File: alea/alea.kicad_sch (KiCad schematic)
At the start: 47 parts, among them J1 QL_SLOT_DIN41612, J2 Conn_02x17_Odd_Even, J3 Conn_01x03_Pin, Q1 BC109, U0 LM340T-5, U1 68000D, U10 MSM514400D, U11 MSM514400D, U12 DP4873V, U2 EP1810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

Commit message: 2025/06 update
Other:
- moved on the sheet: BT1, C1, C2, D1, D2, D3, H1, H2, Q1, R1, R2, U7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

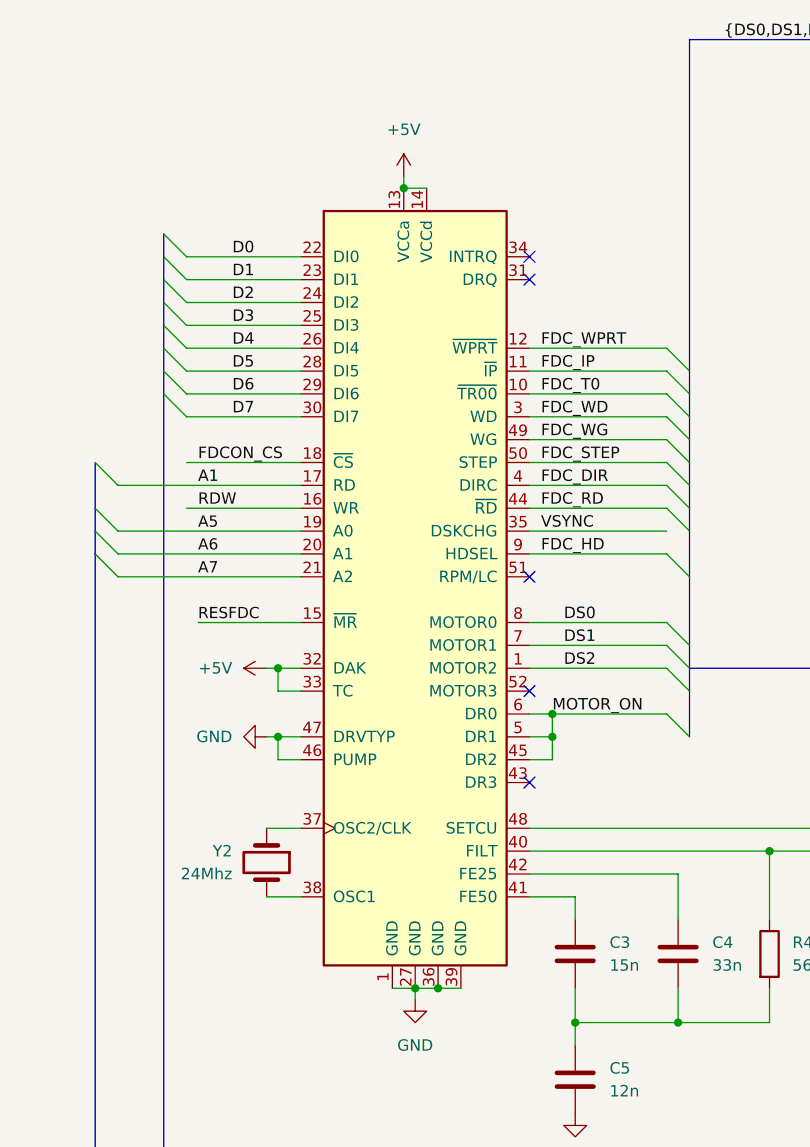
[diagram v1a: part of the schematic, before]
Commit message: update again for bad FDC pinout
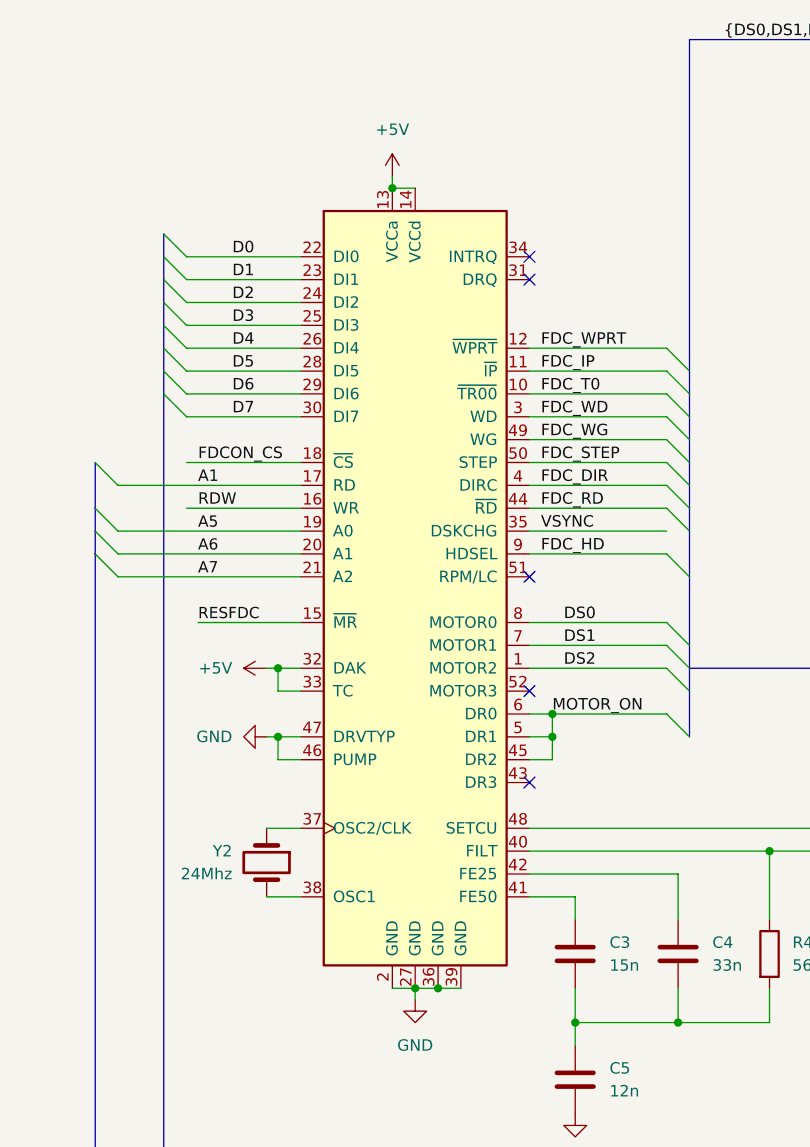
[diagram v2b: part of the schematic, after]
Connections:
- net GND: now also U12.2 (GND); no longer U12.1 (MOTOR2)
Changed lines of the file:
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@@
 	)
 	(junction
-		(at 209.55 81.28)
+		(at 85.09 66.04)
 		(diameter 0)
 		(color 0 0 0 0)
 	)
 	(junction
-		(at 266.7 161.29)
+		(at 209.55 81.28)
 		(diameter 0)
 		(color 0 0 0 0)
 	)
 	(junction
-		(at 86.36 66.04)
+		(at 266.7 161.29)
 		(diameter 0)
 		(color 0 0 0 0)
@@
 	(wire
 		(pts
-			(xy 86.36 64.77) (xy 86.36 66.04)
+			(xy 85.09 64.77) (xy 85.09 66.04)
 		)
 		(stroke
@@
 	(wire
 		(pts
-			(xy 86.36 66.04) (xy 88.9 66.04)
+			(xy 85.09 66.04) (xy 87.63 66.04)
 		)
 		(stroke
@@
 	(symbol
 		(lib_id "GoldCard_Library:+5V")
-		(at 86.36 64.77 0)
+		(at 85.09 64.77 0)
 		(unit 1)
 		(exclude_from_sim no)
@@
 		(fields_autoplaced yes)
 		(property "Reference" "#PWR038"
-			(at 86.36 68.58 0)
+			(at 85.09 68.58 0)
 			(effects
 				(font
@@
 		)
 		(property "Value" "+5V"
-			(at 86.36 59.5376 0)
+			(at 85.09 59.5376 0)
 			(effects
 				(font
@@
 		)
 		(property "Footprint" ""
-			(at 86.36 64.77 0)
+			(at 85.09 64.77 0)
 			(effects
 				(font
@@
 		)
 		(property "Datasheet" ""
-			(at 86.36 64.77 0)
+			(at 85.09 64.77 0)
 			(effects
 				(font
@@
 		)
 		(property "Description" ""
-			(at 86.36 64.77 0)
+			(at 85.09 64.77 0)
 			(effects
 				(font
@@
 		(pin "9"
 		)
-		(pin "1"
+		(pin "2"
 		)
 		(pin "27"

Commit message: fix values
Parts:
- added C17: 100n, Capacitor_THT:C_Disc_D4.3mm_W1.9mm_P5.00mm, symbol GoldCard_Library:C
- C1, C2: value C -> 22p
- Q1: value BC109 -> BC548
- R1, R2: value R -> 1K
- Y3: value Crystal -> 32768hz
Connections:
- net +5V: now also C17.1
- net GND: now also U6.18 (B0)
- net at D1.2 (A), D2.2 (A), U7.8 (GND): now also C17.2
- no-connect marks 43 -> 42
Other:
- title: Sinclair QL Gold Card 3 -> Sinclair QL Gold Card 4 (ALEA's Version)

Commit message: small update in alea
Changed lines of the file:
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@@
 	)
 	(junction
+		(at 64.77 215.9)
+		(diameter 0)
+		(color 0 0 0 0)
+	)
+	(junction
 		(at 209.55 81.28)
 		(diameter 0)
@@
 	)
 	(junction
-		(at 133.35 220.98)
-		(diameter 0)
-		(color 0 0 0 0)
-	)
-	(junction
 		(at 130.81 368.3)
 		(diameter 0)
@@
 	)
 	(junction
-		(at 125.73 220.98)
-		(diameter 0)
-		(color 0 0 0 0)
-	)
-	(junction
 		(at 209.55 114.3)
 		(diameter 0)
@@
 	)
 	(junction
+		(at 64.77 213.36)
+		(diameter 0)
+		(color 0 0 0 0)
+	)
+	(junction
 		(at 35.56 340.36)
 		(diameter 0)
@@
 	)
 	(bus_entry
-		(at 137.16 220.98)
-		(size -2.54 2.54)
-		(stroke
-			(width 0)
-			(type default)
-		)
-	)
-	(bus_entry
 		(at 452.12 81.28)
 		(size 2.54 2.54)
@@
 	)
 	(bus_entry
-		(at 137.16 215.9)
-		(size -2.54 2.54)
-		(stroke
-			(width 0)
-			(type default)
-		)
-	)
-	(bus_entry
 		(at 452.12 125.73)
 		(size 2.54 2.54)
@@
 	)
 	(bus_entry
-		(at 137.16 218.44)
-		(size -2.54 2.54)
-		(stroke
-			(width 0)
-			(type default)
-		)
-	)
-	(bus_entry
 		(at 52.07 238.76)
 		(size 2.54 2.54)
@@
 	(bus
 		(pts
-			(xy 137.16 220.98) (xy 137.16 222.25)
+			(xy 137.16 219.71) (xy 137.16 222.25)
 		)
 		(stroke
@@
 	(wire
 		(pts
-			(xy 54.61 215.9) (xy 92.71 215.9)
+			(xy 54.61 215.9) (xy 64.77 215.9)
 		)
 		(stroke
@@
 		)
 	)
-	(bus
-		(pts
-			(xy 137.16 218.44) (xy 137.16 219.71)
-		)
-		(stroke
-			(width 0)
-			(type default)
-		)
-	)
 	(wire
 		(pts
@@
 		)
 	)
-	(wire
-		(pts
-			(xy 133.35 220.98) (xy 133.35 227.33)
-		)
-		(stroke
-			(width 0)
-			(type default)
-		)
-	)
 	(bus
 		(pts
@@
 		)
 	)
-	(wire
-		(pts
-			(xy 125.73 220.98) (xy 125.73 218.44)
-		)
-		(stroke
-			(width 0)
-			(type default)
-		)
-	)
 	(bus
 		(pts
@@
 		)
 	)
+	(wire
+		(pts
+			(xy 64.77 213.36) (xy 64.77 215.9)
+		)
+		(stroke
+			(width 0)
+			(type default)
+		)
+	)
 	(bus
 		(pts
@@
 		)
 	)
-	(wire
-		(pts
-			(xy 133.35 220.98) (xy 134.62 220.98)
-		)
-		(stroke
-			(width 0)
-			(type default)
-		)
-	)
 	(bus
 		(pts
@@
 	(wire
 		(pts
+			(xy 64.77 215.9) (xy 64.77 222.25)
+		)
+		(stroke
+			(width 0)
+			(type default)
+		)
+	)
+	(wire
+		(pts
 			(xy 407.67 148.59) (xy 420.37 148.59)
 		)
@@
 		)
 	)
+	(wire
+		(pts
+			(xy 64.77 215.9) (xy 92.71 215.9)
+		)
+		(stroke
+			(width 0)
+			(type default)
+		)
+	)
 	(bus
 		(pts
@@
 	(wire
 		(pts
-			(xy 125.73 220.98) (xy 133.35 220.98)
-		)
-		(stroke
-			(width 0)
-			(type default)
-		)
-	)
-	(wire
-		(pts
 			(xy 454.66 270.51) (xy 467.36 270.51)
 		)
@@
 	(wire
 		(pts
-			(xy 54.61 213.36) (xy 92.71 213.36)
+			(xy 54.61 213.36) (xy 64.77 213.36)
 		)
 		(stroke
@@
 		)
 	)
-	(wire
-		(pts
-			(xy 125.73 218.44) (xy 134.62 218.44)
-		)
-		(stroke
-			(width 0)
-			(type default)
-		)
-	)
 	(bus
 		(pts
@@
 		)
 	)
-	(bus
-		(pts
-			(xy 137.16 219.71) (xy 137.16 220.98)
-		)
-		(stroke
-			(width 0)
-			(type default)
-		)
-	)
 	(wire
 		(pts
@@
 		)
 	)
-	(bus
-		(pts
-			(xy 137.16 215.9) (xy 137.16 217.17)
-		)
-		(stroke
-			(width 0)
-			(type default)
-		)
-	)
 	(wire
 		(pts
@@
 	(bus
 		(pts
-			(xy 137.16 214.63) (xy 137.16 215.9)
+			(xy 137.16 214.63) (xy 137.16 217.17)
 		)
 		(stroke
@@
 	(wire
 		(pts
+			(xy 64.77 213.36) (xy 92.71 213.36)
+		)
+		(stroke
+			(width 0)
+			(type default)
+		)
+	)
+	(wire
+		(pts
 			(xy 50.8 344.17) (xy 63.5 344.17)
 		)
@@
 	(bus
 		(pts
-			(xy 137.16 217.17) (xy 137.16 218.44)
+			(xy 137.16 217.17) (xy 137.16 219.71)
 		)
 		(stroke
@@
 		)
 	)
-	(label "A19"
-		(at 129.54 220.98 0)
-		(effects
-			(font
-				(size 1.27 1.27)
-			)
-			(justify left bottom)
-		)
-	)
 	(label "MA5"
 		(at 410.21 151.13 0)
@@
 		)
 	)
-	(label "A18"
-		(at 129.54 218.44 0)
-		(effects
-			(font
-				(size 1.27 1.27)
-			)
-			(justify left bottom)
-		)
-	)
 	(label "RDL"
 		(at 346.71 97.79 0)
@@
 	(symbol
 		(lib_id "GoldCard_Library:GND")
-		(at 133.35 227.33 0)
+		(at 125.73 220.98 90)
 		(unit 1)
 		(exclude_from_sim no)
@@
 		(dnp no)
 		(property "Reference" "#PWR07"
-			(at 133.35 233.68 0)
+			(at 132.08 220.98 0)
 			(effects
 				(font
@@
 		)
 		(property "Value" "GND"
-			(at 135.128 231.14 0)
+			(at 122.682 219.964 90)
 			(effects
 				(font
@@
 		)
 		(property "Footprint" ""
-			(at 133.35 227.33 0)
+			(at 125.73 220.98 0)
 			(effects
 				(font
@@
 		)
 		(property "Datasheet" ""
-			(at 133.35 227.33 0)
+			(at 125.73 220.98 0)
 			(effects
 				(font
@@
 		)
 		(property "Description" ""
-			(at 133.35 227.33 0)
+			(at 125.73 220.98 0)
 			(effects
 				(font
@@
 					(unit 1)
 				)
+			)
+		)
+	)
+	(symbol
+		(lib_id "GoldCard_Library:GND")
+		(at 64.77 222.25 0)
+		(unit 1)
+		(exclude_from_sim no)
+		(in_bom yes)
+		(on_board yes)
+		(dnp no)
+		(property "Reference" "#PWR057"
+			(at 64.77 228.6 0)
+			(effects
+				(font
+					(size 1.27 1.27)
+				)
+				(hide yes)
+			)
+		)
+		(property "Value" "GND"
+			(at 66.548 226.06 0)
+			(effects
+				(font
+					(size 1.27 1.27)
+				)
+				(justify right)
+			)
+		)
+		(property "Footprint" ""
+			(at 64.77 222.25 0)
+			(effects
+				(font
+					(size 1.27 1.27)
+				)
+				(hide yes)
+			)
+		)
+		(property "Datasheet" ""
+			(at 64.77 222.25 0)
+			(effects
+				(font
+					(size 1.27 1.27)
+				)
+				(hide yes)
+			)
+		)
+		(property "Description" ""
+			(at 64.77 222.25 0)
+			(effects
+				(font
+					(size 1.27 1.27)
+				)
+				(hide yes)
+			)
+		)
+		(pin "1"
+		)
+		(instances
+			(project "alea"
+				(path "/aecd9f77-969e-41c8-a7ad-8348a70f1d7d"
+					(reference "#PWR057")
+					(unit 1)
+				)

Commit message: small update in alea
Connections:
- net DG0: now also U8.25 (D3); no longer U8.1 (D0)
- net DG1: now also U8.24 (D2); no longer U8.25 (D3)
- net DG2: now also U8.1 (D0); no longer U8.2 (D1)
- net DG3: now also U8.2 (D1); no longer U8.24 (D2)
- net DG4: now also U9.25 (D3); no longer U9.1 (D0)
- net DG5: now also U9.24 (D2); no longer U9.25 (D3)
- net DG6: now also U9.1 (D0); no longer U9.2 (D1)
- net DG7: now also U9.2 (D1); no longer U9.24 (D2)
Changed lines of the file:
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@@
 	(title_block
 		(title "Sinclair QL Gold Card 4 (ALEA's Version)")
-		(date "2025-07-05")
+		(date "2025-08-06")
 		(rev "0.0")
 		(company "Alvaro Alea Fernandez")
@@
 	)
 	(label "DG1"
-		(at 488.95 73.66 0)
+		(at 488.95 71.12 0)
 		(effects
 			(font
@@
 	)
 	(label "DG5"
-		(at 488.95 135.89 0)
+		(at 488.95 133.35 0)
 		(effects
 			(font
@@
 	)
 	(label "DG4"
-		(at 488.95 128.27 0)
+		(at 488.95 135.89 0)
 		(effects
 			(font
@@
 	)
 	(label "DG0"
-		(at 488.95 66.04 0)
+		(at 488.95 73.66 0)
 		(effects
 			(font
@@
 	)
 	(label "DG2"
-		(at 488.95 68.58 0)
+		(at 488.95 66.04 0)
 		(effects
 			(font
@@
 	)
 	(label "DG7"
-		(at 488.95 133.35 0)
+		(at 488.95 130.81 0)
 		(effects
 			(font
@@
 	)
 	(label "DG3"
-		(at 488.95 71.12 0)
+		(at 488.95 68.58 0)
 		(effects
 			(font
@@
 	)
 	(label "DG6"
-		(at 488.95 130.81 0)
+		(at 488.95 128.27 0)
 		(effects
 			(font
